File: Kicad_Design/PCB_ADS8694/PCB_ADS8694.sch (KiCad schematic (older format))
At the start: 9 parts

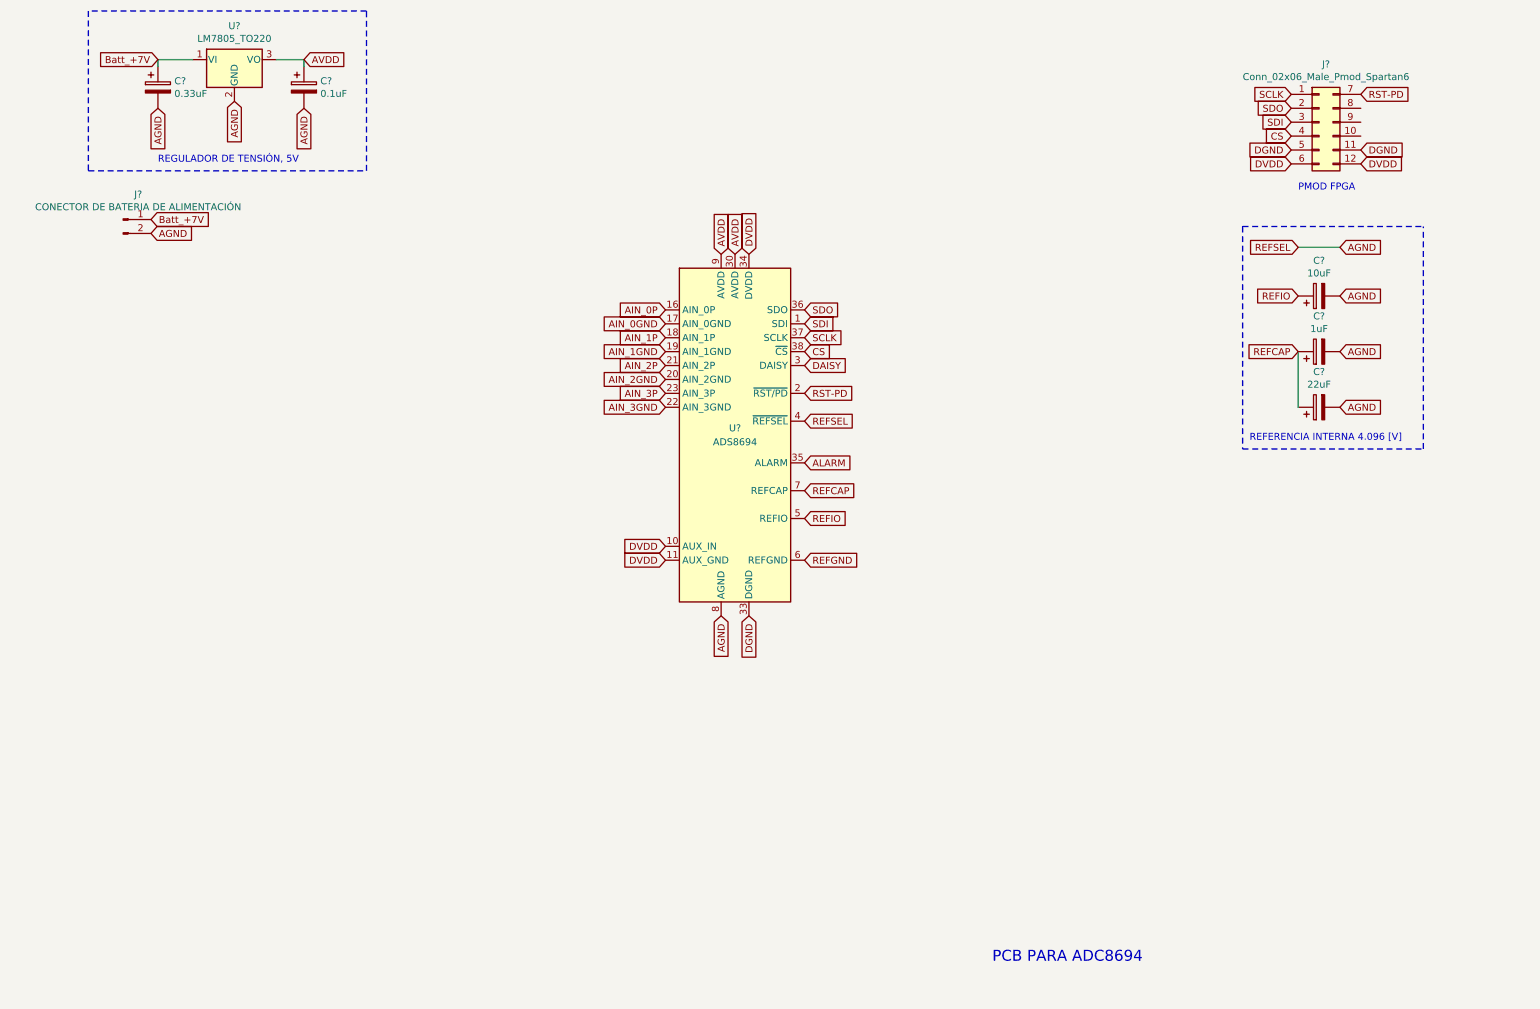
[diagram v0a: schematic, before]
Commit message: Se agrega circuito de seleccion modo daisy-chain
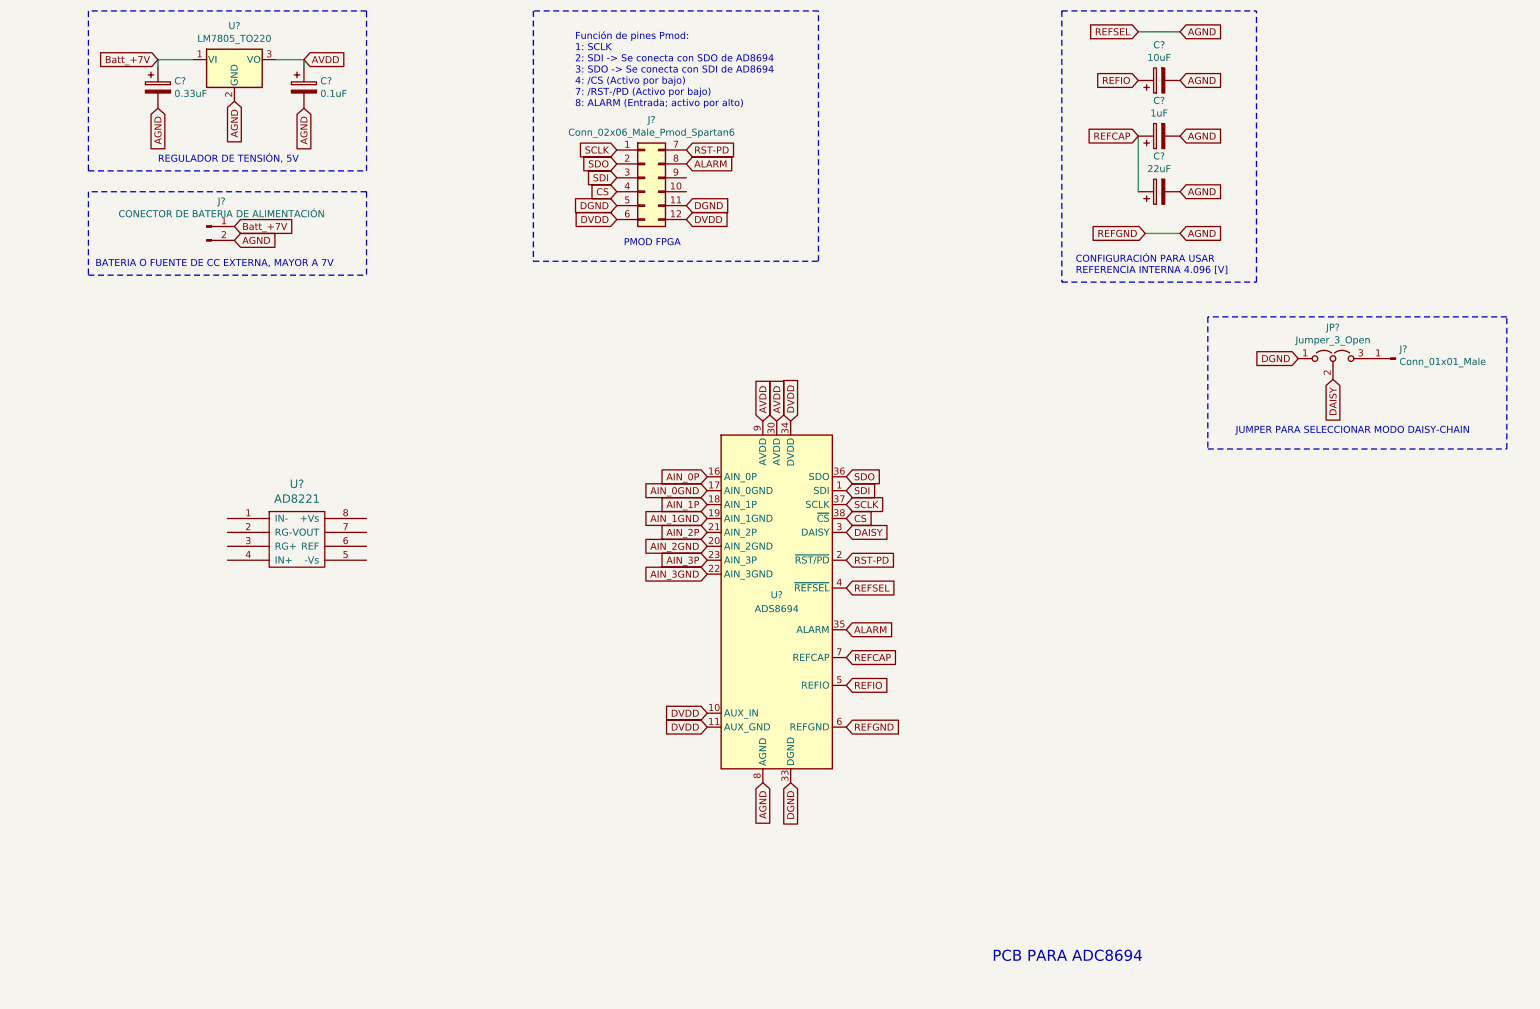
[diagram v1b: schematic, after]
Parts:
- added J?: Conn_01x01_Male, symbol Connector:Conn_01x01_Male
- added JP?: Jumper_3_Open, symbol Jumper:Jumper_3_Open
- added U?: AD8221, symbol Amplifier_Instrumentation:AD8221
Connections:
- net REFGND is gone; now on net AGND: U?.6 (REFGND)
- net ALARM: now also J?.8 (Pin_8)
- net DAISY: now also JP?.2 (C)
- net DGND: now also JP?.1 (A)
- new net: J?.1 (Pin_1), JP?.3 (B)
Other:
- note added: "BATERIA O FUENTE DE CC EXTERNA, MAYOR A 7V"
- note added: "CONFIGURACIÓN PARA USAR\nREFERENCIA INTERNA 4.096 [V]\n"
- note added: "Función de pines Pmod:\n1: SCLK\n2: SDI -> Se conecta con SDO de AD8694\n3: SDO -> Se conecta con SDI de AD8694\n4: /CS (Activo por bajo)\n7: /RST-/PD (Activo por bajo)\n8: ALARM (Entrada; activo por alto)"
- note added: "JUMPER PARA SELECCIONAR MODO DAISY-CHAIN"
- note removed: "REFERENCIA INTERNA 4.096 [V]\n"
- moved on the sheet: C?, J?, U?

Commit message: Se agrega acondicionamiento, entradas analogicas, cambios varios
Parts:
- removed J?: CONECTOR DE BATERIA DE ALIMENTACIÓN, symbol Connector:Conn_01x02_Male
- added C? (x2): 100nf, symbol Device:C
- added J?: Conn_01x03_Male_Alimentación_analógica_externa_(+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, symbol Connector:Conn_01x03_Male
- added J? (x2): Conn_01x04_Female_Entradas_analógicas_diferencial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, symbol Connector:Conn_01x04_Female
- added R?: 38C (24.3k), symbol Device:R
- added RV?: R_POT_TRIM_US_100k, symbol Device:R_POT_TRIM_US
- added U?: AD8221, symbol Amplifier_Instrumentation:AD8221
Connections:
- net labels added: +VCC, -VCC, AIN_0+, AIN_0-, AIN_1+, AIN_1-, GNDA, GNDD
- net labels removed: AGND, AIN_0GND, AIN_1GND, AIN_2GND, AIN_3GND, Batt_+7V, REFGND
- wire segments 7 -> 46
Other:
- note added: "ACONDICIONAMIENTO, CANAL DIFERENCIAL 0\nRESISTENCIA SMD 1% 24.3k, GANANCIA FIJA DE 3"
- note added: "ACONDICIONAMIENTO, CANAL DIFERENCIAL 1\nGANANCIA VARIABLE, TRIMMER 100k\n\n"
- note added: "BATERIA O FUENTE DE CC EXTERNA, +-VCC"
- note added: "PCB ADC8694"
- note removed: "BATERIA O FUENTE DE CC EXTERNA, MAYOR A 7V"
- note removed: "PCB PARA ADC8694"
- moved on the sheet: U?

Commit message: Se agregan AD8221 en los 4 canales
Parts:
- removed J? (x2): Conn_01x04_Female_Entradas_analógicas_diferencial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, symbol Connector:Conn_01x04_Female
- removed R?: 38C (24.3k), symbol Device:R
- removed U?: AD8221, symbol Amplifier_Instrumentation:AD8221
- added J?: Conn_01x08_Female_Entradas, symbol Connector:Conn_01x08_Female
- added RV? (x3): R_POT_TRIM_US_100k, symbol Device:R_POT_TRIM_US
- added U? (x3): AD8221, symbol Amplifier_Instrumentation:AD8221
- gave numbers to parts that had none: 15
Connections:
- net labels added: AIN_2+, AIN_2-, AIN_3+, AIN_3-
- net labels removed: DGND
- wire segments 46 -> 64
- no-connect marks 0 -> 2
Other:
- note added: "ACONDICIONAMIENTO, CANAL DIFERENCIAL 0\nGANANCIA VARIABLE, TRIMMER 100k\n\n"
- note removed: "ACONDICIONAMIENTO, CANAL DIFERENCIAL 0\nRESISTENCIA SMD 1% 24.3k, GANANCIA FIJA DE 3"
- note removed: "ACONDICIONAMIENTO, CANAL DIFERENCIAL 1\nGANANCIA VARIABLE, TRIMMER 100k\n\n"
- moved on the sheet: C5, C6, C7, J5, JP1, RV1, U3, U4

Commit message: Se agrega AD8221 en 4 canales, se agrega pin para daisy chain
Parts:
- removed J5: Conn_01x01_Male, symbol Connector:Conn_01x01_Male
- removed J?: Conn_01x08_Female_Entradas, symbol Connector:Conn_01x08_Female
- added C10, C8, C9: C, symbol Device:C
- added J2: Conn_01x10_Female, symbol Connector:Conn_01x10_Female
- added J?: Conn_01x02_Male, symbol Connector:Conn_01x02_Male
- added R1, R2, R3: R, symbol Device:R
- J1: value Conn_01x03_Male_Alimentación_analógica_externa_(+-12V) -> Conn_01x03_Male_Alimentación_analógica_externa_(+-VCC)
- RV1: value R_POT_TRIM_US_100k -> R_POT_TRIM_US
- RV2, RV3: renamed from RV?; value R_POT_TRIM_US_100k -> R_POT_TRIM_US
- gave numbers to parts that had none: 4
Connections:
- net labels added: AUX_IN
- wire segments 64 -> 71
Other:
- note added: "ACONDICIONAMIENTO CON FILTRO PASA BAJO RC"
- note added: "COMUNICACIÓN SPI\nFunción de pines Pmod:\n1: SCLK\n2: SDI -> Se conecta con SDO de AD8694\n3: SDO -> Se conecta con SDI de AD8694\n4: /CS (Activo por bajo)\n7: /RST-/PD (Activo por bajo)\n8: ALARM (Entrada; activo por alto)"
- note added: "ENTRADA CON ACONDICIONAMIENTO SIN FILTRO RC"
- note added: "FUENTE DE CC EXTERNA, +-VCC"
- note added: "PIN DAISY"
- note added: "PIN SDO\n"
- note removed: "ACONDICIONAMIENTO, CANAL DIFERENCIAL 0\nGANANCIA VARIABLE, TRIMMER 100k\n\n"
- note removed: "BATERIA O FUENTE DE CC EXTERNA, +-VCC"
- note removed: "Función de pines Pmod:\n1: SCLK\n2: SDI -> Se conecta con SDO de AD8694\n3: SDO -> Se conecta con SDI de AD8694\n4: /CS (Activo por bajo)\n7: /RST-/PD (Activo por bajo)\n8: ALARM (Entrada; activo por alto)"
- moved on the sheet: RV1, RV2, RV3, RV4, U2, U3, U4, U5, U6

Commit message: Se agrega informacion, primer version terminada
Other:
- note added: "ENTRADAS"
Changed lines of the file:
@@
 	4600 3700 4600 3900
 Connection ~ 4600 3900
-Text GLabel 1650 3700 2    50   Input ~ 0
+Text GLabel 1650 3650 2    50   Input ~ 0
 AIN_3-
-Text GLabel 1650 3800 2    50   Input ~ 0
+Text GLabel 1650 3750 2    50   Input ~ 0
 AIN_3+
-Text GLabel 1650 3900 2    50   Input ~ 0
+Text GLabel 1650 3850 2    50   Input ~ 0
 AIN_2-
-Text GLabel 1650 4000 2    50   Input ~ 0
+Text GLabel 1650 3950 2    50   Input ~ 0
 AIN_2+
 $Comp
@@
 	8700 3925 9100 3925
 Connection ~ 8450 3975
-Text GLabel 1650 4100 2    50   Input ~ 0
+Text GLabel 1650 4050 2    50   Input ~ 0
 AIN_1-
-Text GLabel 1650 4200 2    50   Input ~ 0
+Text GLabel 1650 4150 2    50   Input ~ 0
 AIN_1+
-Text GLabel 1650 4300 2    50   Input ~ 0
+Text GLabel 1650 4250 2    50   Input ~ 0
 AIN_0-
-Text GLabel 1650 4400 2    50   Input ~ 0
+Text GLabel 1650 4350 2    50   Input ~ 0
 AIN_0+
 Wire Wire Line
@@
 L Connector:Conn_01x10_Female J2
 U 1 1 5CD7A7C7
-P 1450 4000
-F 0 "J2" H 1600 4000 50  0000 C CNN
-F 1 "Conn_01x10_Female" H 1342 3366 50  0000 C CNN
-F 2 "" H 1450 4000 50  0001 C CNN
-F 3 "~" H 1450 4000 50  0001 C CNN
-	1    1450 4000
+P 1450 3950
+F 0 "J2" H 1600 3950 50  0000 C CNN
+F 1 "Conn_01x10_Female" H 1342 3316 50  0000 C CNN
+F 2 "" H 1450 3950 50  0001 C CNN
+F 3 "~" H 1450 3950 50  0001 C CNN
+	1    1450 3950
 	-1   0    0    1
 $EndComp
@@
 L power:GNDA #PWR01
 U 1 1 5CD81712
-P 2100 3500
-F 0 "#PWR01" H 2100 3250 50  0001 C CNN
-F 1 "GNDA" H 2105 3327 50  0000 C CNN
-F 2 "" H 2100 3500 50  0001 C CNN
-F 3 "" H 2100 3500 50  0001 C CNN
-	1    2100 3500
-	1    0    0    -1
-$EndComp
-Text GLabel 1650 3600 2    50   Input ~ 0
+P 2100 3450
+F 0 "#PWR01" H 2100 3200 50  0001 C CNN
+F 1 "GNDA" H 2105 3277 50  0000 C CNN
+F 2 "" H 2100 3450 50  0001 C CNN
+F 3 "" H 2100 3450 50  0001 C CNN
+	1    2100 3450
+	1    0    0    -1
+$EndComp
+Text GLabel 1650 3550 2    50   Input ~ 0
 AUX_IN
 Wire Wire Line
-	1650 3500 2100 3500
+	1650 3450 2100 3450
 Wire Notes Line
 	950  4550 2350 4550
@@
 Wire Notes Line
 	7800 3300 7800 4600
+Text Notes 1500 4500 0    50   ~ 0
+ENTRADAS
 $EndSCHEMATC

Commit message: cambios de alimentación
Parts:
- gave numbers to parts that had none: 1
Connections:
- net labels added: VCC, VDD, VSS
- net labels removed: +VCC, -VCC, DVDD
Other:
- moved on the sheet: RV4, U6

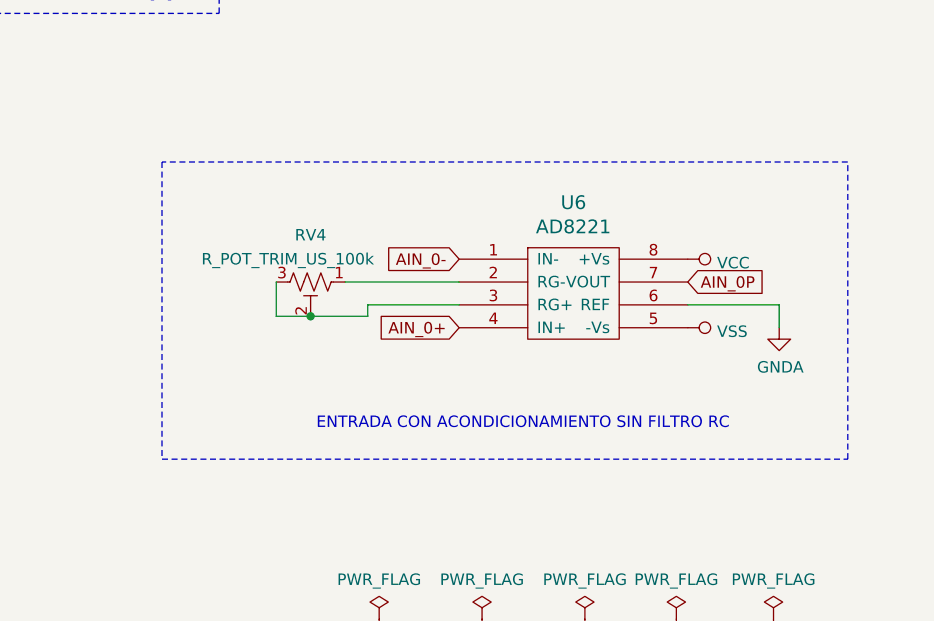
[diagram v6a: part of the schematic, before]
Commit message: Agregado de capacitor para filtrar componente de CC en canal 0
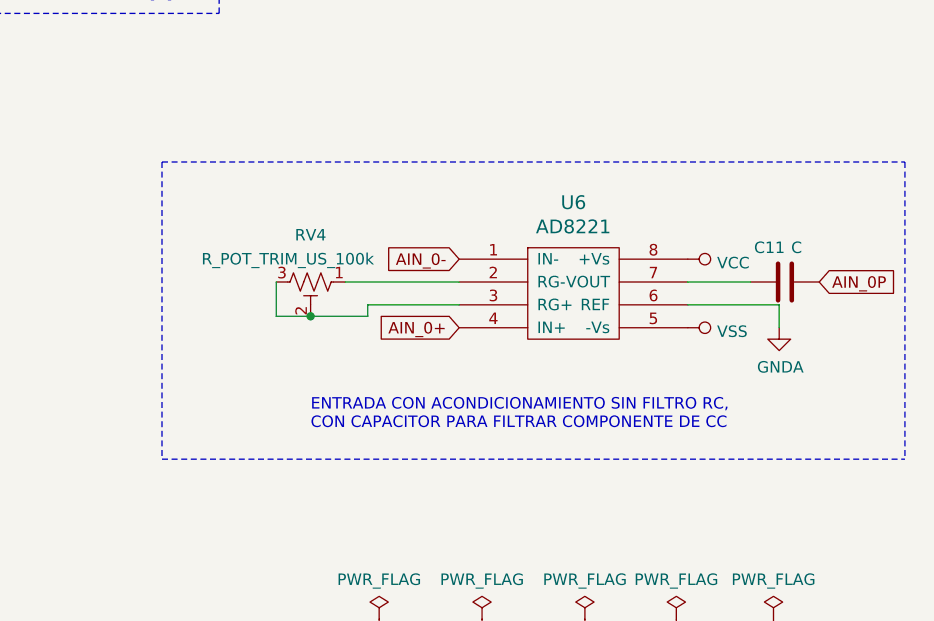
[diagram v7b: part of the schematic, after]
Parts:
- added C11: C, symbol Device:C
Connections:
- wire segments 71 -> 72
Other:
- note added: "ENTRADA CON ACONDICIONAMIENTO SIN FILTRO RC, \nCON CAPACITOR PARA FILTRAR COMPONENTE DE CC"
- note removed: "ENTRADA CON ACONDICIONAMIENTO SIN FILTRO RC"
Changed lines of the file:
@@
 Wire Wire Line
 	10500 3875 10100 3875
-Text GLabel 10100 3775 2    50   Input ~ 0
+Text GLabel 10675 3775 2    50   Input ~ 0
 AIN_0P
 Text GLabel 9100 3975 0    50   Input ~ 0
@@
 	950  3250 950  4550
 Wire Notes Line
-	600  7750 4000 7750
-Wire Notes Line
-	4000 7750 4000 4700
-Wire Notes Line
 	4000 4700 600  4700
 Wire Notes Line
@@
 Wire Notes Line
 	8750 1700 11025 1700
-Text Notes 8475 4425 0    50   ~ 0
-ENTRADA CON ACONDICIONAMIENTO SIN FILTRO RC
-Wire Notes Line
-	7800 4550 10800 4550
-Wire Notes Line
-	10800 4550 10800 3250
-Wire Notes Line
-	10800 3250 7800 3250
+Text Notes 8450 4425 0    50   ~ 0
+ENTRADA CON ACONDICIONAMIENTO SIN FILTRO RC, \nCON CAPACITOR PARA FILTRAR COMPONENTE DE CC
 Wire Notes Line
 	7800 3250 7800 4550
@@
 Text GLabel 5250 3600 0    50   Input ~ 0
 AIN_0P
+$Comp
+L Device:C C11
+U 1 1 5CD98B94
+P 10525 3775
+F 0 "C11" V 10675 3775 50  0000 L CNN
+F 1 "C" V 10675 3700 50  0000 L CNN
+F 2 "" H 10563 3625 50  0001 C CNN
+F 3 "~" H 10525 3775 50  0001 C CNN
+	1    10525 3775
+	0    -1   -1   0
+$EndComp
+Wire Wire Line
+	10375 3775 10100 3775
+Wire Notes Line
+	11050 3250 11050 4550
+Wire Notes Line
+	7800 4550 11050 4550
+Wire Notes Line
+	7800 3250 11050 3250
+Wire Notes Line
+	4000 7750 4000 4700
+Wire Notes Line
+	600  7750 4000 7750
 $EndSCHEMATC

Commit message: Asignacion de huellas
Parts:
- C1: footprint (none) -> Capacitor_THT:CP_Radial_D4.0mm_P2.00mm
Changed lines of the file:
@@
 F 0 "C1" H 1568 1246 50  0000 L CNN
 F 1 "0.33uF" H 1568 1155 50  0000 L CNN
-F 2 "" H 1488 1050 50  0001 C CNN
+F 2 "Capacitor_THT:CP_Radial_D4.0mm_P2.00mm" H 1488 1050 50  0001 C CNN
 F 3 "~" H 1450 1200 50  0001 C CNN
 	1    1450 1200
